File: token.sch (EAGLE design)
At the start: 9 parts

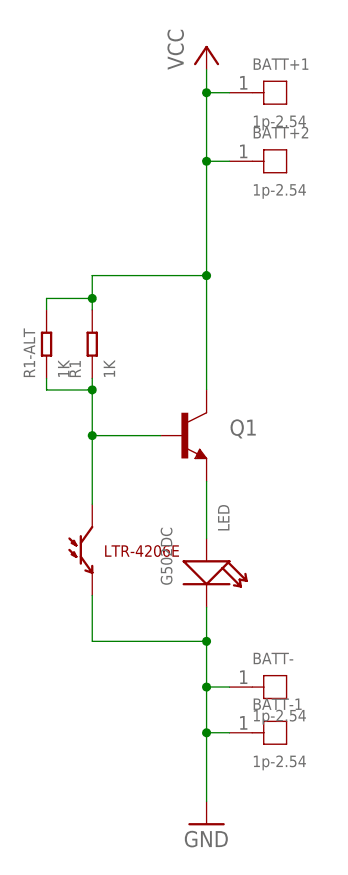
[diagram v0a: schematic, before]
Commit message: Added PCB art
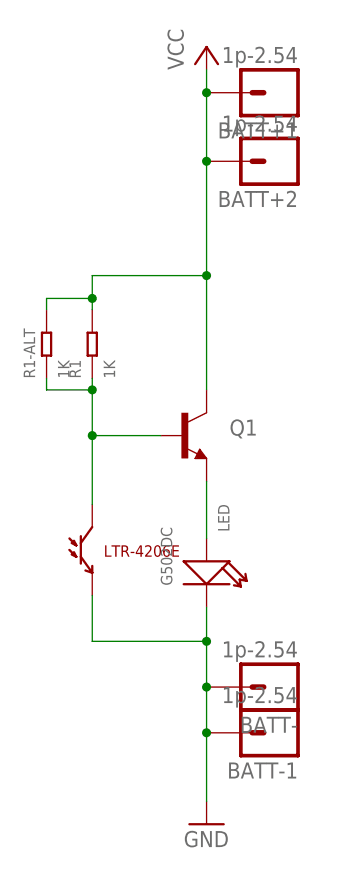
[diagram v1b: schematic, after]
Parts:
- BATT+1, BATT+2, BATT-, BATT-1: device Seeed-OPL-Connector:DIP-BLACK-ROUND-FEMALE-HEADER-VERT(1P-2.54) -> SparkFun-Connectors:M01NOSILK-KIT
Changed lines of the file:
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@@
 <?xml version="1.0" encoding="utf-8"?>
 <!DOCTYPE eagle SYSTEM "eagle.dtd">
-<eagle version="8.2.2">
+<eagle version="8.0.0">
 <drawing>
 <settings>
@@
 <part name="LTR-4206E" library="SparkFun-Sensors" deviceset="LTR-301" device=""/>
 <part name="R1-ALT" library="Seeed-OPL-Resistor" deviceset="SMD-RES-0.1R-5%-1/8W(0805)" device="" value="1K"/>
-<part name="BATT+1" library="Seeed-OPL-Connector" deviceset="DIP-BLACK-ROUND-FEMALE-HEADER-VERT(1P-2.54)" device="" value="1p-2.54"/>
-<part name="BATT-" library="Seeed-OPL-Connector" deviceset="DIP-BLACK-ROUND-FEMALE-HEADER-VERT(1P-2.54)" device="" value="1p-2.54"/>
-<part name="BATT+2" library="Seeed-OPL-Connector" deviceset="DIP-BLACK-ROUND-FEMALE-HEADER-VERT(1P-2.54)" device="" value="1p-2.54"/>
-<part name="BATT-1" library="Seeed-OPL-Connector" deviceset="DIP-BLACK-ROUND-FEMALE-HEADER-VERT(1P-2.54)" device="" value="1p-2.54"/>
+<part name="BATT+1" library="SparkFun-Connectors" deviceset="M01" device="NOSILK-KIT" value="1p-2.54"/>
+<part name="BATT-" library="SparkFun-Connectors" deviceset="M01" device="NOSILK-KIT" value="1p-2.54"/>
+<part name="BATT+2" library="SparkFun-Connectors" deviceset="M01" device="NOSILK-KIT" value="1p-2.54"/>
+<part name="BATT-1" library="SparkFun-Connectors" deviceset="M01" device="NOSILK-KIT" value="1p-2.54"/>
 </parts>
 <sheets>
@@
 <instance part="LTR-4206E" gate="G$1" x="71.12" y="25.4"/>
 <instance part="R1-ALT" gate="G$1" x="66.04" y="45.72" rot="R90"/>
-<instance part="BATT+1" gate="G$1" x="91.44" y="73.66"/>
-<instance part="BATT-" gate="G$1" x="91.44" y="7.62"/>
-<instance part="BATT+2" gate="G$1" x="91.44" y="66.04"/>
-<instance part="BATT-1" gate="G$1" x="91.44" y="2.54"/>
+<instance part="BATT+1" gate="G$1" x="91.44" y="73.66" rot="R180"/>
+<instance part="BATT-" gate="G$1" x="91.44" y="7.62" rot="R180"/>
+<instance part="BATT+2" gate="G$1" x="91.44" y="66.04" rot="R180"/>
+<instance part="BATT-1" gate="G$1" x="91.44" y="2.54" rot="R180"/>
 </instances>
 <busses>
@@
 <junction x="83.82" y="12.7"/>
 <pinref part="BATT-" gate="G$1" pin="1"/>
-<wire x1="86.36" y1="7.62" x2="83.82" y2="7.62" width="0.1524" layer="91"/>
 <junction x="83.82" y="7.62"/>
 <pinref part="BATT-1" gate="G$1" pin="1"/>
-<wire x1="86.36" y1="2.54" x2="83.82" y2="2.54" width="0.1524" layer="91"/>
 <junction x="83.82" y="2.54"/>
 </segment>
@@
 <junction x="71.12" y="50.8"/>
 <pinref part="BATT+1" gate="G$1" pin="1"/>
-<wire x1="86.36" y1="73.66" x2="83.82" y2="73.66" width="0.1524" layer="91"/>
 <junction x="83.82" y="73.66"/>
 <pinref part="BATT+2" gate="G$1" pin="1"/>
-<wire x1="86.36" y1="66.04" x2="83.82" y2="66.04" width="0.1524" layer="91"/>
 <junction x="83.82" y="66.04"/>
 </segment>

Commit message: Initial wiring and routing
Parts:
- removed BATT+1, BATT+2, BATT-, BATT-1: 1p-2.54, SparkFun-Connectors:M01NOSILK-KIT
- removed LTR-4206E: (no value), SparkFun-Sensors:LTR-301
- removed Q1: (no value), SparkFun-DiscreteSemi:TRANSISTOR_NPN2N3904
- removed R1: 1K, Seeed-OPL-Resistor:DIP-RES-1K-5%-1/4W(PR-D2.3XL6.5MM)
- removed R1-ALT: 1K, Seeed-OPL-Resistor:SMD-RES-0.1R-5%-1/8W(0805)
- added D1, D2, D3, D4, D6, D7, D8: (no value), adafruit:LEDSQR2X5
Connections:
- removed net GND: BATT-.1, BATT-1.1, LED.-, LTR-4206E.E
- removed net VCC: BATT+1.1, BATT+2.1, Q1.C, R1-ALT.2, R1.2
- new net N$45: D2.C, D3.A
- new net N$48: D3.C, D4.A
- new net N$51: D4.C, LED.+
- new net N$54: D6.A, LED.-
- new net N$59: D6.C, D7.A
- new net N$65: D7.C, D8.A
- net N$1: now also D1.A, D8.C; no longer LED.+, Q1.E
- net N$2: now also D1.C, D2.A; no longer LTR-4206E.C, Q1.B, R1-ALT.1, R1.1
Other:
- moved on the sheet: LED
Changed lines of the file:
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@@
 <?xml version="1.0" encoding="utf-8"?>
 <!DOCTYPE eagle SYSTEM "eagle.dtd">
-<eagle version="8.0.0">
+<eagle version="8.2.2">
 <drawing>
 <settings>
@@
 </classes>
 <parts>
-<part name="P+1" library="supply1" deviceset="VCC" device=""/>
-<part name="GND1" library="supply1" deviceset="GND" device=""/>
-<part name="Q1" library="SparkFun-DiscreteSemi" deviceset="TRANSISTOR_NPN" device="2N3904"/>
 <part name="LED" library="Seeed-OPL-Diode" deviceset="DIP-LED-GREEN-GREEN(2P-D5MM)" device="" value="G502DC"/>
-<part name="R1" library="Seeed-OPL-Resistor" deviceset="DIP-RES-1K-5%-1/4W(PR-D2.3XL6.5MM)" device="" value="1K"/>
-<part name="LTR-4206E" library="SparkFun-Sensors" deviceset="LTR-301" device=""/>
-<part name="R1-ALT" library="Seeed-OPL-Resistor" deviceset="SMD-RES-0.1R-5%-1/8W(0805)" device="" value="1K"/>
-<part name="BATT+1" library="SparkFun-Connectors" deviceset="M01" device="NOSILK-KIT" value="1p-2.54"/>
-<part name="BATT-" library="SparkFun-Connectors" deviceset="M01" device="NOSILK-KIT" value="1p-2.54"/>
-<part name="BATT+2" library="SparkFun-Connectors" deviceset="M01" device="NOSILK-KIT" value="1p-2.54"/>
-<part name="BATT-1" library="SparkFun-Connectors" deviceset="M01" device="NOSILK-KIT" value="1p-2.54"/>
+<part name="D1" library="adafruit" deviceset="LED" device="SQR2X5"/>
+<part name="D2" library="adafruit" deviceset="LED" device="SQR2X5"/>
+<part name="D3" library="adafruit" deviceset="LED" device="SQR2X5"/>
+<part name="D4" library="adafruit" deviceset="LED" device="SQR2X5"/>
+<part name="D6" library="adafruit" deviceset="LED" device="SQR2X5"/>
+<part name="D7" library="adafruit" deviceset="LED" device="SQR2X5"/>
+<part name="D8" library="adafruit" deviceset="LED" device="SQR2X5"/>
 </parts>
 <sheets>
@@
 </plain>
 <instances>
-<instance part="P+1" gate="VCC" x="83.82" y="78.74"/>
-<instance part="GND1" gate="1" x="83.82" y="-7.62"/>
-<instance part="Q1" gate="G$1" x="81.28" y="35.56"/>
-<instance part="LED" gate="G$1" x="83.82" y="20.32" rot="R270"/>
-<instance part="R1" gate="G$1" x="71.12" y="45.72" rot="R90"/>
-<instance part="LTR-4206E" gate="G$1" x="71.12" y="25.4"/>
-<instance part="R1-ALT" gate="G$1" x="66.04" y="45.72" rot="R90"/>
-<instance part="BATT+1" gate="G$1" x="91.44" y="73.66" rot="R180"/>
-<instance part="BATT-" gate="G$1" x="91.44" y="7.62" rot="R180"/>
-<instance part="BATT+2" gate="G$1" x="91.44" y="66.04" rot="R180"/>
-<instance part="BATT-1" gate="G$1" x="91.44" y="2.54" rot="R180"/>
+<instance part="LED" gate="G$1" x="182.88" y="25.4" rot="R180"/>
+<instance part="D1" gate="G$1" x="195.58" y="68.58"/>
+<instance part="D2" gate="G$1" x="195.58" y="58.42"/>
+<instance part="D3" gate="G$1" x="195.58" y="48.26"/>
+<instance part="D4" gate="G$1" x="195.58" y="38.1"/>
+<instance part="D6" gate="G$1" x="170.18" y="45.72" rot="R180"/>
+<instance part="D7" gate="G$1" x="170.18" y="55.88" rot="R180"/>
+<instance part="D8" gate="G$1" x="170.18" y="66.04" rot="R180"/>
 </instances>
 <busses>
@@
 <net name="N$1" class="0">
 <segment>
-<pinref part="Q1" gate="G$1" pin="E"/>
+<pinref part="D8" gate="G$1" pin="C"/>
+<wire x1="170.18" y1="71.12" x2="170.18" y2="76.2" width="0.1524" layer="91"/>
+<pinref part="D1" gate="G$1" pin="A"/>
+<wire x1="170.18" y1="76.2" x2="195.58" y2="76.2" width="0.1524" layer="91"/>
+<wire x1="195.58" y1="76.2" x2="195.58" y2="71.12" width="0.1524" layer="91"/>
+</segment>
+</net>
+<net name="N$2" class="0">
+<segment>
+<pinref part="D1" gate="G$1" pin="C"/>
+<pinref part="D2" gate="G$1" pin="A"/>
+<wire x1="195.58" y1="63.5" x2="195.58" y2="60.96" width="0.1524" layer="91"/>
+</segment>
+</net>
+<net name="N$45" class="0">
+<segment>
+<pinref part="D2" gate="G$1" pin="C"/>
+<pinref part="D3" gate="G$1" pin="A"/>
+<wire x1="195.58" y1="53.34" x2="195.58" y2="50.8" width="0.1524" layer="91"/>
+</segment>
+</net>
+<net name="N$48" class="0">
+<segment>
+<pinref part="D3" gate="G$1" pin="C"/>
+<pinref part="D4" gate="G$1" pin="A"/>
+<wire x1="195.58" y1="43.18" x2="195.58" y2="40.64" width="0.1524" layer="91"/>
+</segment>
+</net>
+<net name="N$51" class="0">
+<segment>
+<pinref part="D4" gate="G$1" pin="C"/>
+<wire x1="195.58" y1="33.02" x2="195.58" y2="25.4" width="0.1524" layer="91"/>
 <pinref part="LED" gate="G$1" pin="+"/>
-<wire x1="83.82" y1="30.48" x2="83.82" y2="24.13" width="0.1524" layer="91"/>
-</segment>
-</net>
-<net name="GND" class="0">
+<wire x1="195.58" y1="25.4" x2="186.69" y2="25.4" width="0.1524" layer="91"/>
+</segment>
+</net>
+<net name="N$54" class="0">
 <segment>
 <pinref part="LED" gate="G$1" pin="-"/>
-<pinref part="GND1" gate="1" pin="GND"/>
-<wire x1="83.82" y1="16.51" x2="83.82" y2="12.7" width="0.1524" layer="91"/>
-<pinref part="LTR-4206E" gate="G$1" pin="E"/>
-<wire x1="83.82" y1="12.7" x2="83.82" y2="7.62" width="0.1524" layer="91"/>
-<wire x1="83.82" y1="7.62" x2="83.82" y2="2.54" width="0.1524" layer="91"/>
-<wire x1="83.82" y1="2.54" x2="83.82" y2="-5.08" width="0.1524" layer="91"/>
-<wire x1="71.12" y1="17.78" x2="71.12" y2="12.7" width="0.1524" layer="91"/>
-<wire x1="71.12" y1="12.7" x2="83.82" y2="12.7" width="0.1524" layer="91"/>
-<junction x="83.82" y="12.7"/>
-<pinref part="BATT-" gate="G$1" pin="1"/>
-<junction x="83.82" y="7.62"/>
-<pinref part="BATT-1" gate="G$1" pin="1"/>
-<junction x="83.82" y="2.54"/>
-</segment>
-</net>
-<net name="N$2" class="0">
-<segment>
-<pinref part="R1" gate="G$1" pin="1"/>
-<pinref part="LTR-4206E" gate="G$1" pin="C"/>
-<wire x1="71.12" y1="41.91" x2="71.12" y2="40.64" width="0.1524" layer="91"/>
-<pinref part="Q1" gate="G$1" pin="B"/>
-<wire x1="71.12" y1="40.64" x2="71.12" y2="35.56" width="0.1524" layer="91"/>
-<wire x1="71.12" y1="35.56" x2="71.12" y2="27.94" width="0.1524" layer="91"/>
-<wire x1="78.74" y1="35.56" x2="71.12" y2="35.56" width="0.1524" layer="91"/>
-<junction x="71.12" y="35.56"/>
-<pinref part="R1-ALT" gate="G$1" pin="1"/>
-<wire x1="66.04" y1="41.91" x2="66.04" y2="40.64" width="0.1524" layer="91"/>
-<wire x1="66.04" y1="40.64" x2="71.12" y2="40.64" width="0.1524" layer="91"/>
-<junction x="71.12" y="40.64"/>
-</segment>
-</net>
-<net name="VCC" class="0">
-<segment>
-<pinref part="Q1" gate="G$1" pin="C"/>
-<pinref part="P+1" gate="VCC" pin="VCC"/>
-<wire x1="83.82" y1="40.64" x2="83.82" y2="53.34" width="0.1524" layer="91"/>
-<pinref part="R1" gate="G$1" pin="2"/>
-<wire x1="83.82" y1="53.34" x2="83.82" y2="66.04" width="0.1524" layer="91"/>
-<wire x1="83.82" y1="66.04" x2="83.82" y2="73.66" width="0.1524" layer="91"/>
-<wire x1="83.82" y1="73.66" x2="83.82" y2="76.2" width="0.1524" layer="91"/>
-<wire x1="71.12" y1="49.53" x2="71.12" y2="50.8" width="0.1524" layer="91"/>
-<wire x1="71.12" y1="50.8" x2="71.12" y2="53.34" width="0.1524" layer="91"/>
-<wire x1="71.12" y1="53.34" x2="83.82" y2="53.34" width="0.1524" layer="91"/>
-<junction x="83.82" y="53.34"/>
-<pinref part="R1-ALT" gate="G$1" pin="2"/>
-<wire x1="71.12" y1="50.8" x2="66.04" y2="50.8" width="0.1524" layer="91"/>
-<wire x1="66.04" y1="50.8" x2="66.04" y2="49.53" width="0.1524" layer="91"/>
-<junction x="71.12" y="50.8"/>
-<pinref part="BATT+1" gate="G$1" pin="1"/>
-<junction x="83.82" y="73.66"/>
-<pinref part="BATT+2" gate="G$1" pin="1"/>
-<junction x="83.82" y="66.04"/>
-</segment>
-</net>
+<wire x1="179.07" y1="25.4" x2="170.18" y2="25.4" width="0.1524" layer="91"/>
+<pinref part="D6" gate="G$1" pin="A"/>
+<wire x1="170.18" y1="25.4" x2="170.18" y2="43.18" width="0.1524" layer="91"/>
+</segment>
+</net>
+<net name="N$59" class="0">
+<segment>
+<pinref part="D6" gate="G$1" pin="C"/>
+<pinref part="D7" gate="G$1" pin="A"/>
+<wire x1="170.18" y1="50.8" x2="170.18" y2="53.34" width="0.1524" layer="91"/>
+</segment>
+</net>
+<net name="N$65" class="0">
+<segment>
+<pinref part="D7" gate="G$1" pin="C"/>
+<pinref part="D8" gate="G$1" pin="A"/>
+<wire x1="170.18" y1="60.96" x2="170.18" y2="63.5" width="0.1524" layer="91"/>
+</segment>
+</net>
